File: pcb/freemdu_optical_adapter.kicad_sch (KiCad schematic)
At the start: 19 parts, among them J1 Conn_01x04, J2 Conn_01x04, J3 Conn_01x07, J4 Conn_01x07, J5 Conn_01x02, J6 Conn_01x04, Q1 BSS138, Q2 BSS138, U1 SFH7250, U3 74LVC1G17GW,125

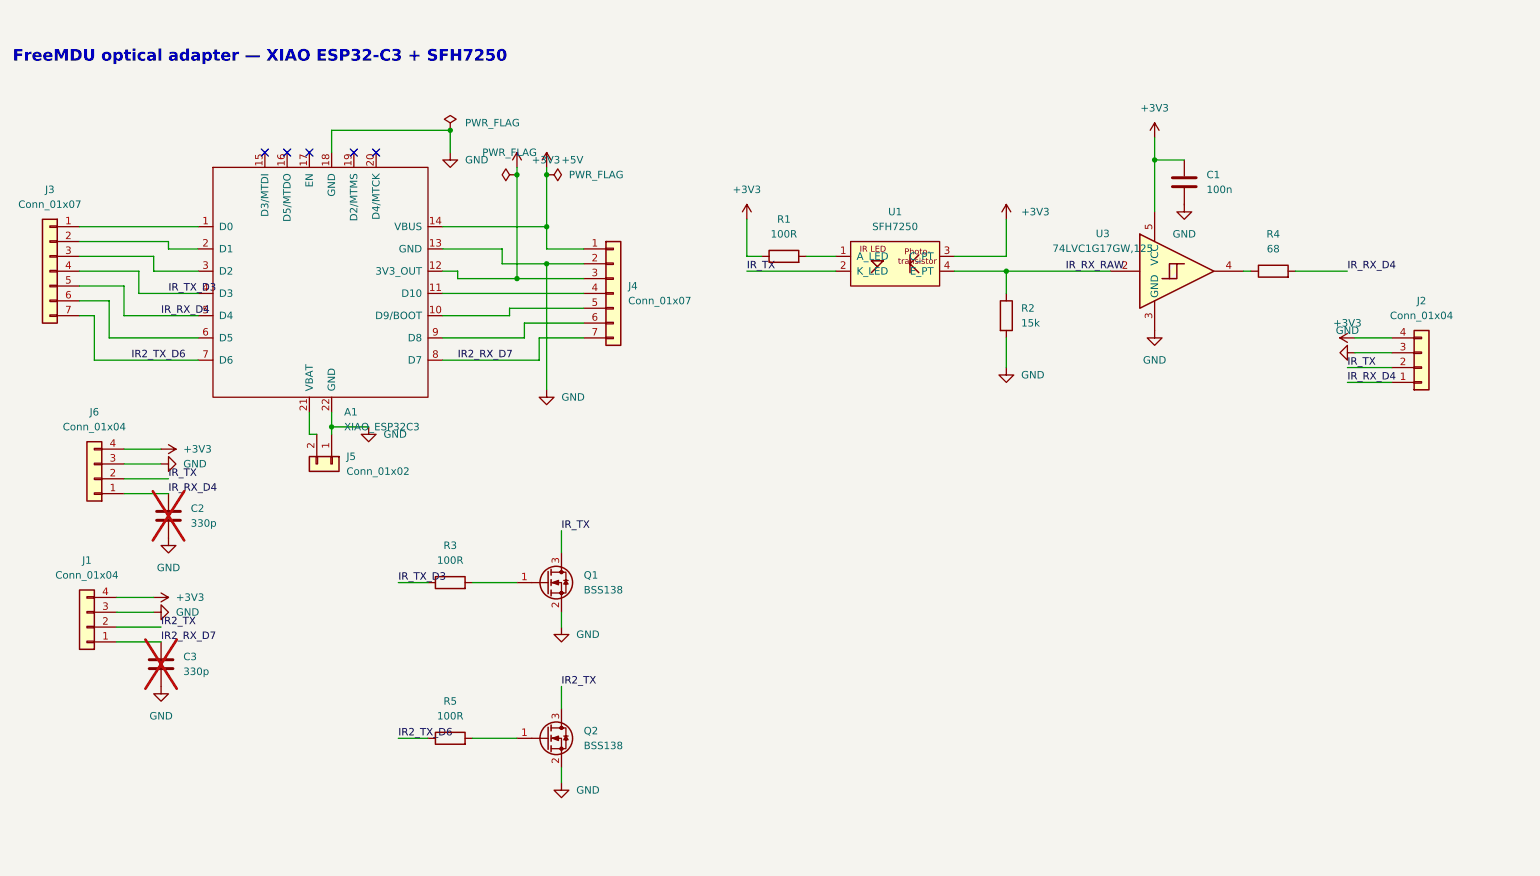
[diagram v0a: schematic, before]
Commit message: update PCB with optional simple schematic
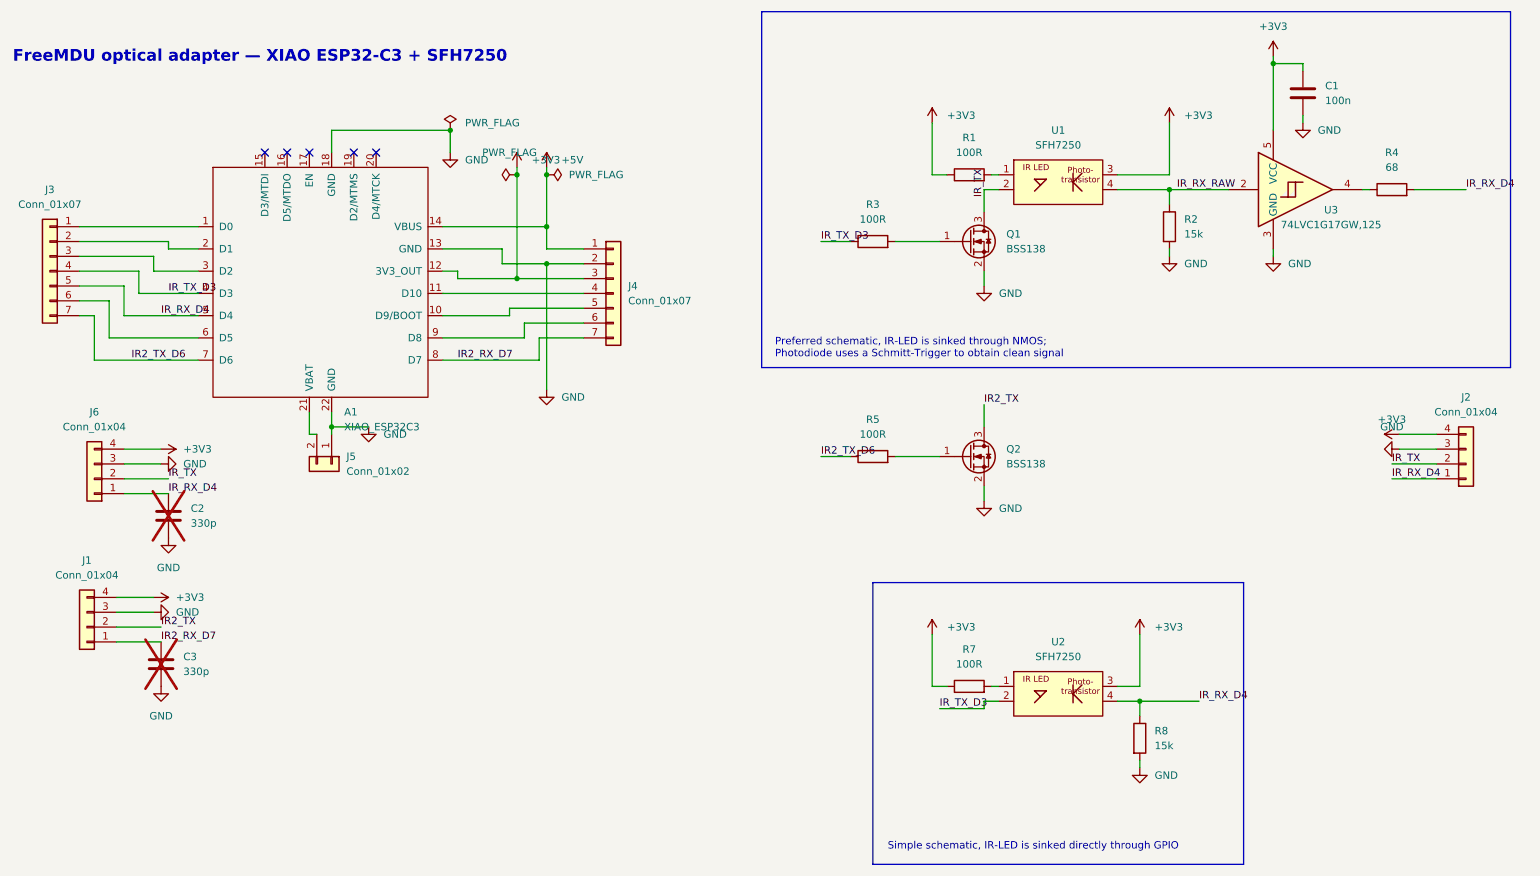
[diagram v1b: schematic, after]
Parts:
- added R7: 100R, Resistor_SMD:R_0805_2012Metric_Pad1.20x1.40mm_HandSolder, symbol Device:R
- added R8: 15k, Resistor_SMD:R_0805_2012Metric_Pad1.20x1.40mm_HandSolder, symbol Device:R
- added U2: SFH7250, FreeMDU_Optics:SFH7250_Multi_TOPLED, symbol FreeMDU_Optics:SFH7250
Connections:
- net +3V3: now also R7.1, U2.3 (C_PT)
- net GND: now also R8.2
- net IR_RX_D4: now also R8.1, U2.4 (E_PT)
- net IR_TX_D3: now also U2.2 (K_LED)
- new net: R7.2, U2.1 (A_LED)
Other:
- note added: "Preferred schematic, IR-LED is sinked through NMOS; Photodiode uses a Schmitt-Trigger to obtain clean signal"
- note added: "Simple schematic, IR-LED is sinked directly through GPIO"
- moved on the sheet: C1, J2, Q1, Q2, R1, R2, R3, R4, R5, U3

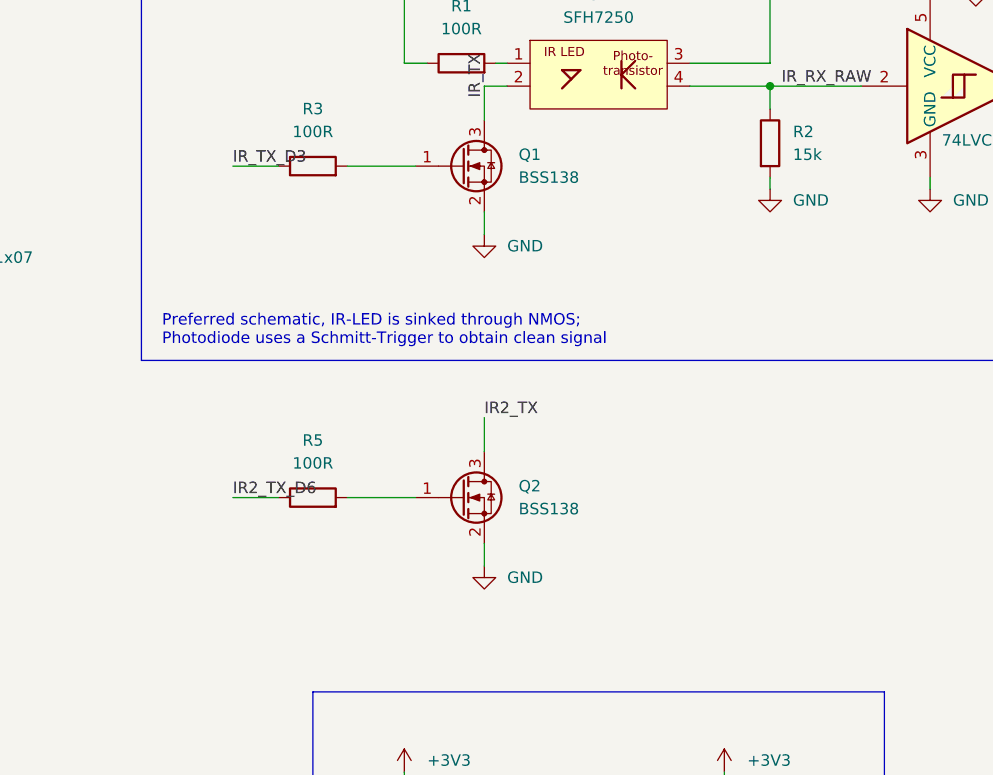
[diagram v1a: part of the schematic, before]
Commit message: fix missing pulldowns for nmos-gates
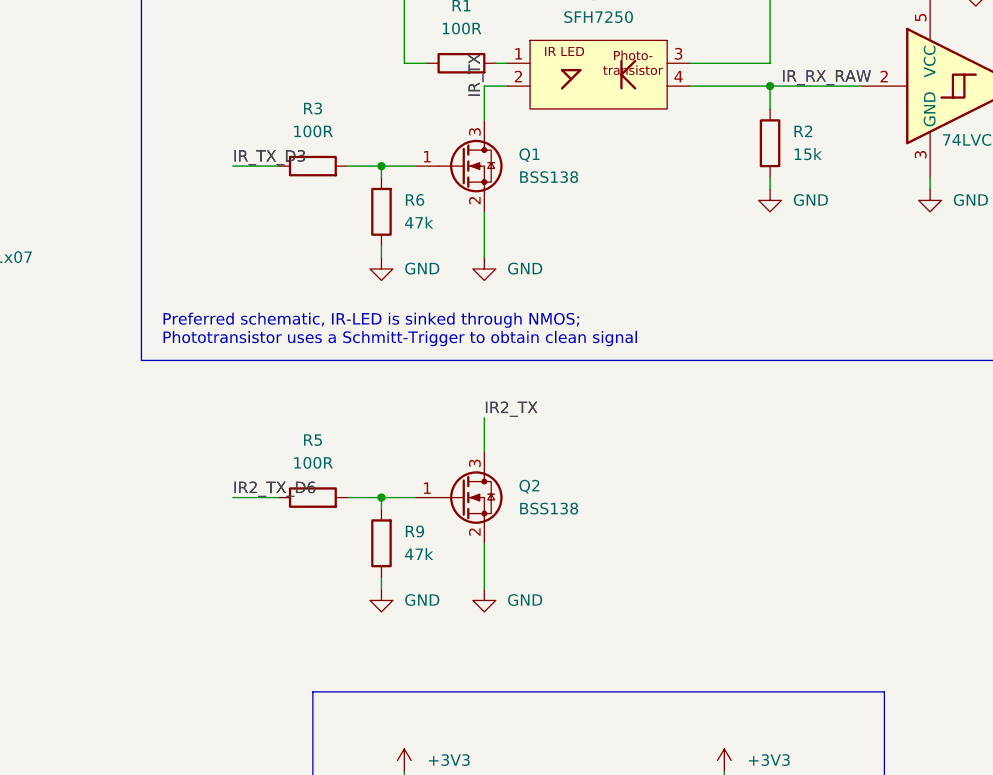
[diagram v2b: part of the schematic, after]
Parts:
- added R6, R9: 47k, Resistor_SMD:R_0805_2012Metric_Pad1.20x1.40mm_HandSolder, symbol Device:R
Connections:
- net GND: now also R6.1, R9.1
- net at Q1.1 (G), R3.2: now also R6.2
- net at Q2.1 (G), R5.2: now also R9.2
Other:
- note added: "Preferred schematic, IR-LED is sinked through NMOS; Phototransistor uses a Schmitt-Trigger to obtain clean signal"
- note removed: "Preferred schematic, IR-LED is sinked through NMOS; Photodiode uses a Schmitt-Trigger to obtain clean signal"
